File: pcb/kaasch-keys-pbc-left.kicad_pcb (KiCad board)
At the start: 2 copper layers, 163.1 x 125 mm, 73 parts, among them J1 Conn_01x12_Pin, J2 Conn_01x12_Pin, SW1 SW_Push, SW10 SW_Push, SW11 SW_Push, SW12 SW_Push, SW13 SW_Push, SW14 SW_Push, SW15 SW_Push, SW16 SW_Push, SW17 SW_Push, SW18 SW_Push, SW19 SW_Push, SW2 SW_Push, SW20 SW_Push, SW21 SW_Push, SW22 SW_Push, SW23 SW_Push, SW24 SW_Push, SW25 SW_Push, SW26 SW_Push, SW27 SW_Push, SW28 SW_Push, SW29 SW_Push, SW3 SW_Push, SW30 SW_Push, SW31 SW_Push, SW32 SW_Push, SW33 SW_Push, SW34 SW_Push, SW35 SW_Push, SW36 SW_Push_Reset, SW4 SW_Push, SW5 SW_Push, SW6 SW_Push, SW7 SW_Push, SW8 SW_Push, SW9 SW_Push

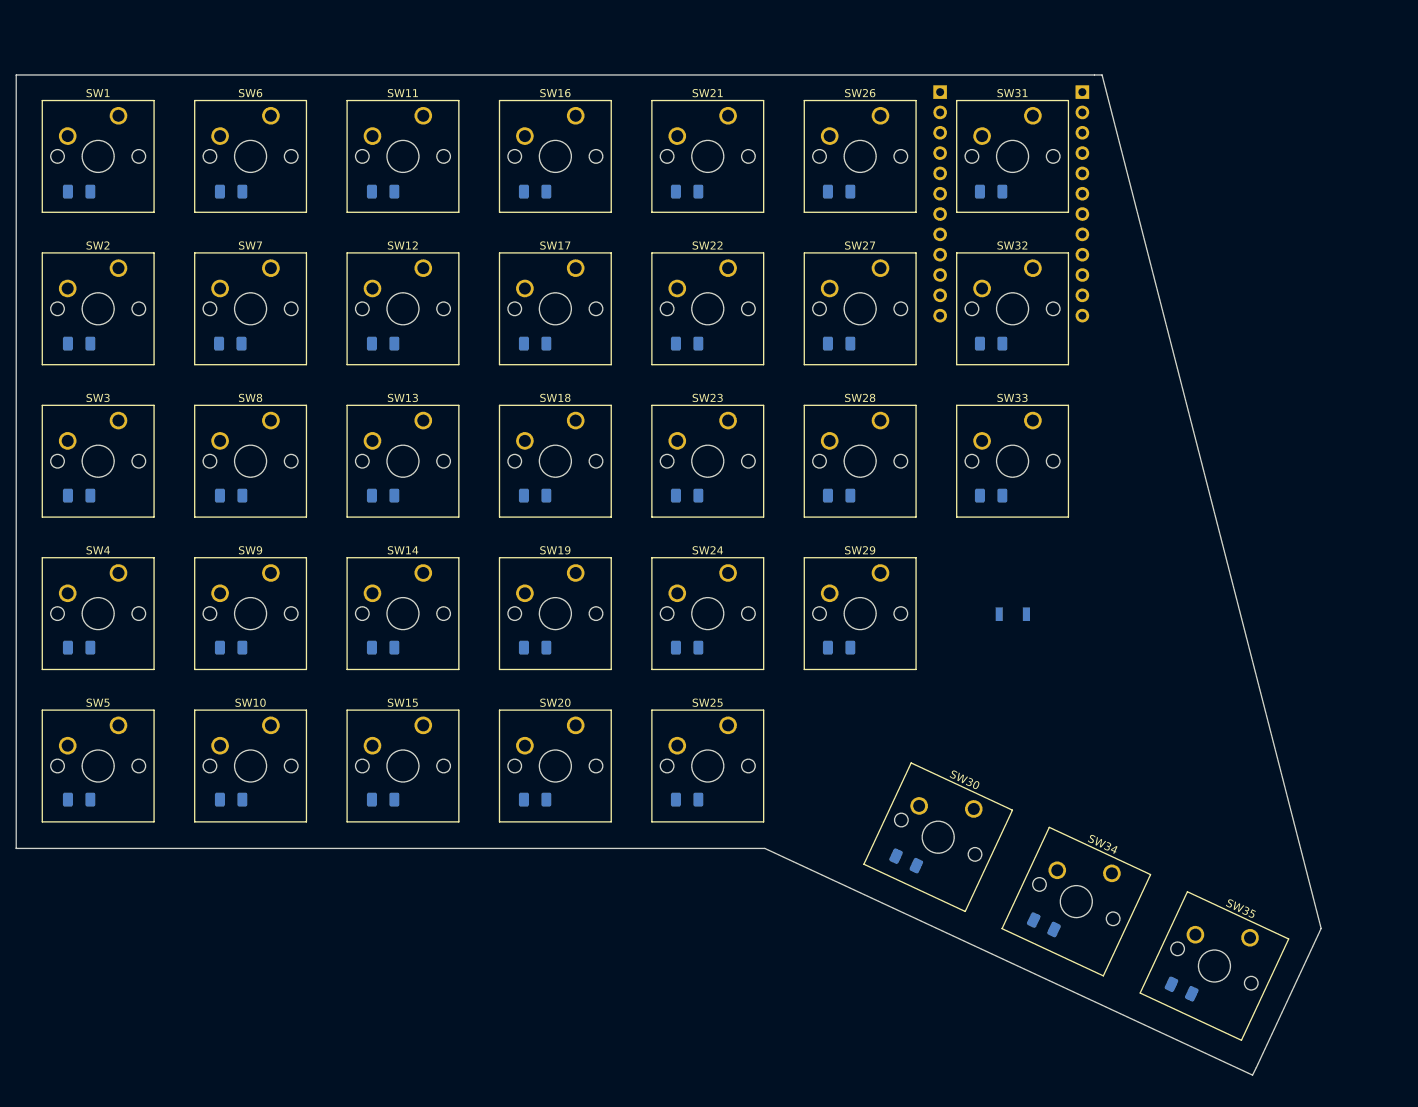
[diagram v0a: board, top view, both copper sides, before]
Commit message: left pcb complete and ready for testing
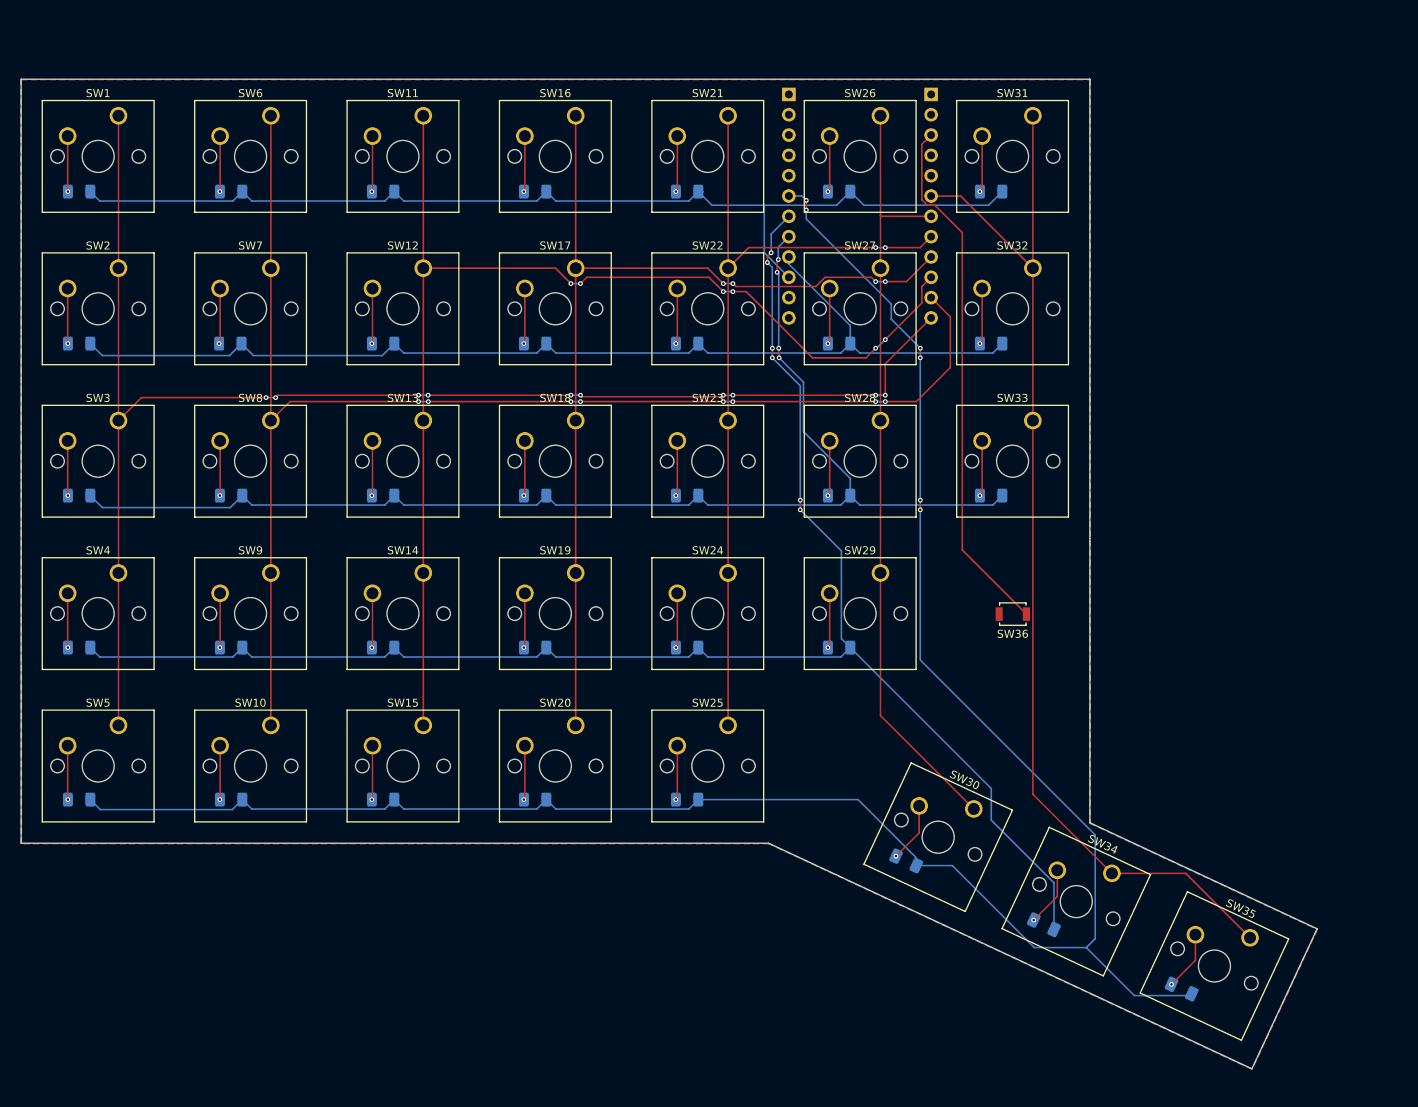
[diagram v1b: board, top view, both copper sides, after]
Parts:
- SW36: moved to F.Cu
- moved J1 18.9 mm to (157.1, 44.1)
- moved J2 18.9 mm to (174.8, 44.1)
- turned SW36 to 180 degrees
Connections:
- J1 pad 3: unconnected-(J1-Pin_3-Pad3) -> GND
- J1 pad 4: unconnected-(J1-Pin_4-Pad4) -> GND
- J2 pad 2: Net-(J2-Pin_2) -> GND
- SW36 pad 1: Net-(J2-Pin_2) -> Net-(J2-Pin_3)
- SW36 pad 2: Net-(J2-Pin_3) -> GND
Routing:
- net row.4.L: track 0.00 -> 263.7 mm, vias 0 -> 6
- net row.3.L: track 0.00 -> 205.0 mm, vias 0 -> 6
- net col.0.L: track 0.00 -> 185.6 mm, vias 0 -> 10
- net col.1.L: track 0.00 -> 173.6 mm, vias 0 -> 8
- net row.2.L: track 0.00 -> 156.9 mm, vias 0 -> 4
- net col.2.L: track 0.00 -> 150.4 mm, vias 0 -> 6
- net col.6.L: track 0.00 -> 135.8 mm
- net row.1.L: track 0.00 -> 134.4 mm
- net row.0.L: track 0.00 -> 131.6 mm
- net col.3.L: track 0.00 -> 123.6 mm, vias 0 -> 4
- net col.4.L: track 0.00 -> 103.2 mm, vias 0 -> 2
- net col.5.L: track 0.00 -> 97.8 mm
- net Net-(J2-Pin_3): track 0.00 -> 66.3 mm
- net Net-(D30-A): track 0.00 -> 7.48 mm, vias 0 -> 1
- net Net-(D34-A): track 0.00 -> 7.44 mm, vias 0 -> 1
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- added copper zone on B.Cu, net GND
- added copper zone on F.Cu, net GND
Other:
- board size 163.1 x 125 mm -> 162 x 123.7 mm

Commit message: alternative thumb cluster position
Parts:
- SW30, SW34: footprint Button_Switch_Keyboard:SW_Cherry_MX_1.00u_PCB -> Button_Switch_Keyboard:SW_Cherry_MX_1.50u_PCB
- moved SW30 12.7 mm to (167.5, 134.5), turned to 65 degrees
- moved SW34 12.7 mm to (184.7, 142.5), turned to 65 degrees
- moved SW35 9.22 mm to (208.0, 155.8)
- moved D35 9.22 mm to (199.4, 162.2)
- moved D34 3.85 mm to (191.2, 151.0), turned to -115 degrees
- moved D30 3.76 mm to (174.0, 142.9), turned to -115 degrees
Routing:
- net row.4.L: track 263.7 -> 0.00 mm, vias 6 -> 0
- net row.3.L: track 205.0 -> 0.00 mm, vias 6 -> 0
- net col.0.L: track 185.6 -> 0.00 mm, vias 10 -> 0
- net col.1.L: track 173.6 -> 0.00 mm, vias 8 -> 0
- net row.2.L: track 156.9 -> 0.00 mm, vias 4 -> 0
- net col.2.L: track 150.4 -> 0.00 mm, vias 6 -> 0
- net col.6.L: track 135.8 -> 0.00 mm
- net row.1.L: track 134.4 -> 0.00 mm
- net row.0.L: track 131.6 -> 0.00 mm
- net col.3.L: track 123.6 -> 0.00 mm, vias 4 -> 0
- net col.4.L: track 103.2 -> 0.00 mm, vias 2 -> 0
- net col.5.L: track 97.8 -> 0.00 mm
- net Net-(J2-Pin_3): track 66.3 -> 0.00 mm
- net Net-(D30-A): track 7.48 -> 0.00 mm, vias 1 -> 0
- net Net-(D34-A): track 7.44 -> 0.00 mm, vias 1 -> 0
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- removed copper zone on B.Cu, net GND
- removed copper zone on F.Cu, net GND
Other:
- board outline removed

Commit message: finished new layout
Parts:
- moved SW30 19.6 mm to (185.0, 125.6)
- moved D30 19.6 mm to (191.5, 134.1)
- moved SW34 19.6 mm to (202.3, 133.7)
- moved SW35 19.6 mm to (225.5, 147.0)
- moved D34 19.6 mm to (208.7, 142.2)
- moved D35 19.6 mm to (216.9, 153.4)
- moved SW36 19.4 mm to (202.7, 101.0)
- moved SW16 19.4 mm to (148.1, 38.8)
- moved SW18 19.4 mm to (148.1, 76.9)
- moved SW19 19.4 mm to (148.1, 95.9)
- moved SW20 19.4 mm to (148.1, 115.0)
- moved SW31 19.4 mm to (205.2, 38.8)
- moved SW33 19.4 mm to (205.2, 76.9)
- moved SW17 19.4 mm to (148.1, 57.8)
- moved SW32 19.4 mm to (205.2, 57.8)
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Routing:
- net row.4.L: track 0.00 -> 226.3 mm
- net row.3.L: track 0.00 -> 200.1 mm, vias 0 -> 2
- net col.0.L: track 0.00 -> 183.3 mm
- net col.1.L: track 0.00 -> 167.4 mm, vias 0 -> 2
- net row.2.L: track 0.00 -> 151.3 mm, vias 0 -> 2
- net col.2.L: track 0.00 -> 146.2 mm, vias 0 -> 2
- net col.6.L: track 0.00 -> 140.9 mm
- net row.0.L: track 0.00 -> 135.4 mm
- net row.1.L: track 0.00 -> 129.8 mm, vias 0 -> 2
- net col.3.L: track 0.00 -> 126.5 mm, vias 0 -> 2
- net col.4.L: track 0.00 -> 106.3 mm, vias 0 -> 2
- net col.5.L: track 0.00 -> 93.8 mm, vias 0 -> 2
- net Net-(J2-Pin_3): track 0.00 -> 62.7 mm
- net Net-(D30-A): track 0.00 -> 7.48 mm, vias 0 -> 1
- net Net-(D34-A): track 0.00 -> 7.44 mm, vias 0 -> 1
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- added copper zone on B.Cu, net GND
- added copper zone on F.Cu, net GND
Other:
- board outline added: 154.8 x 128.9 mm

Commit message: iterations
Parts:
- moved J1 37.5 mm to (212.2, 38.1)
- moved J2 34.9 mm to (227.4, 38.1)
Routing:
- net col.5.L: track 93.8 -> 162.3 mm, vias 2 -> 0
- net col.4.L: track 106.3 -> 169.0 mm
- net col.3.L: track 126.5 -> 187.4 mm
- net col.2.L: track 146.2 -> 204.0 mm
- net col.0.L: track 183.3 -> 238.5 mm, vias 0 -> 2
- net col.1.L: track 167.4 -> 221.6 mm
- net row.2.L: track 151.3 -> 185.7 mm
- net row.3.L: track 200.1 -> 232.1 mm
- net col.6.L: track 140.9 -> 172.4 mm
- net row.4.L: track 226.3 -> 253.7 mm, vias 0 -> 2
- net Net-(J2-Pin_3): track 62.7 -> 77.8 mm, vias 0 -> 1
- net row.0.L: track 135.4 -> 146.6 mm
- net row.1.L: track 129.8 -> 134.3 mm, vias 2 -> 0
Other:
- outline, holes or cut-outs redrawn
